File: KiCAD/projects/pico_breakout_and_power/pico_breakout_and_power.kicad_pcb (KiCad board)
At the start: 2 copper layers, 3 parts, among them J1 Conn_01x17_Socket, J12 Conn_01x17_Socket

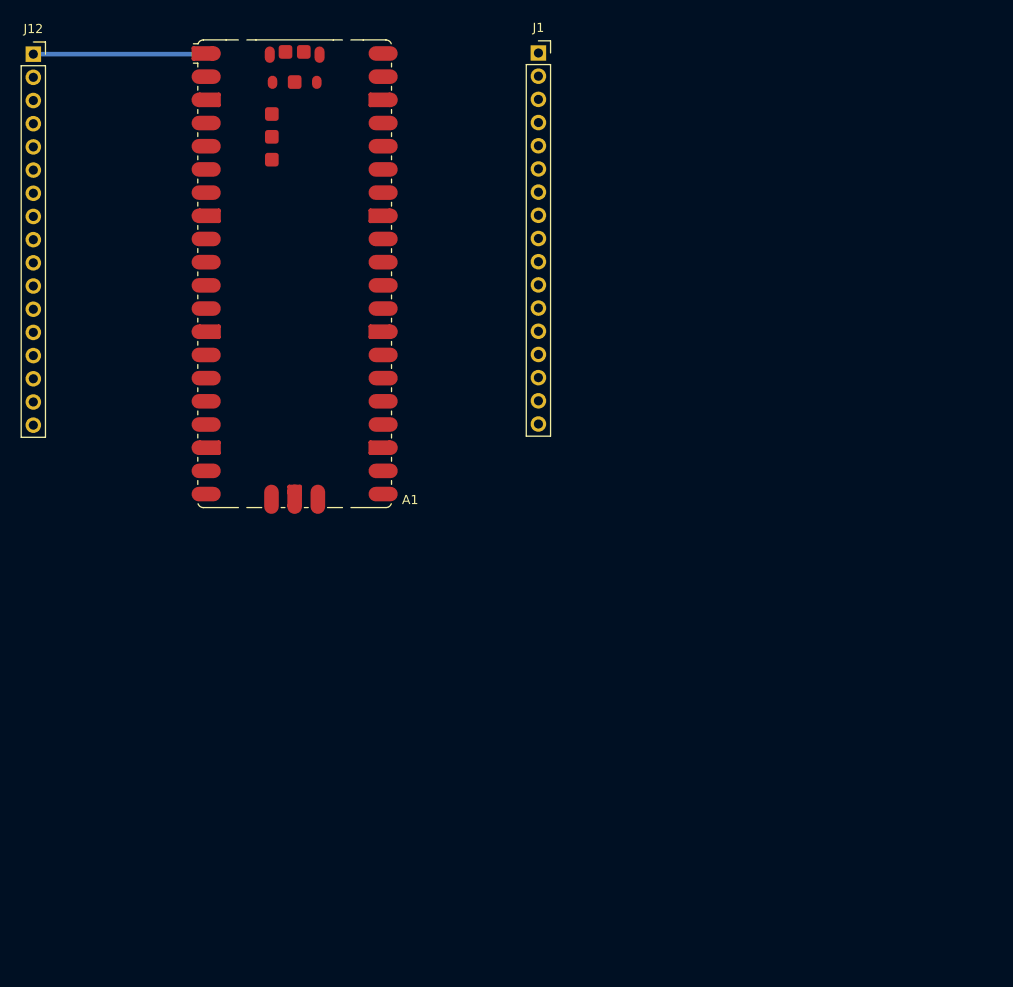
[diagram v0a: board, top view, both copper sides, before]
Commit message: Add proper board edge
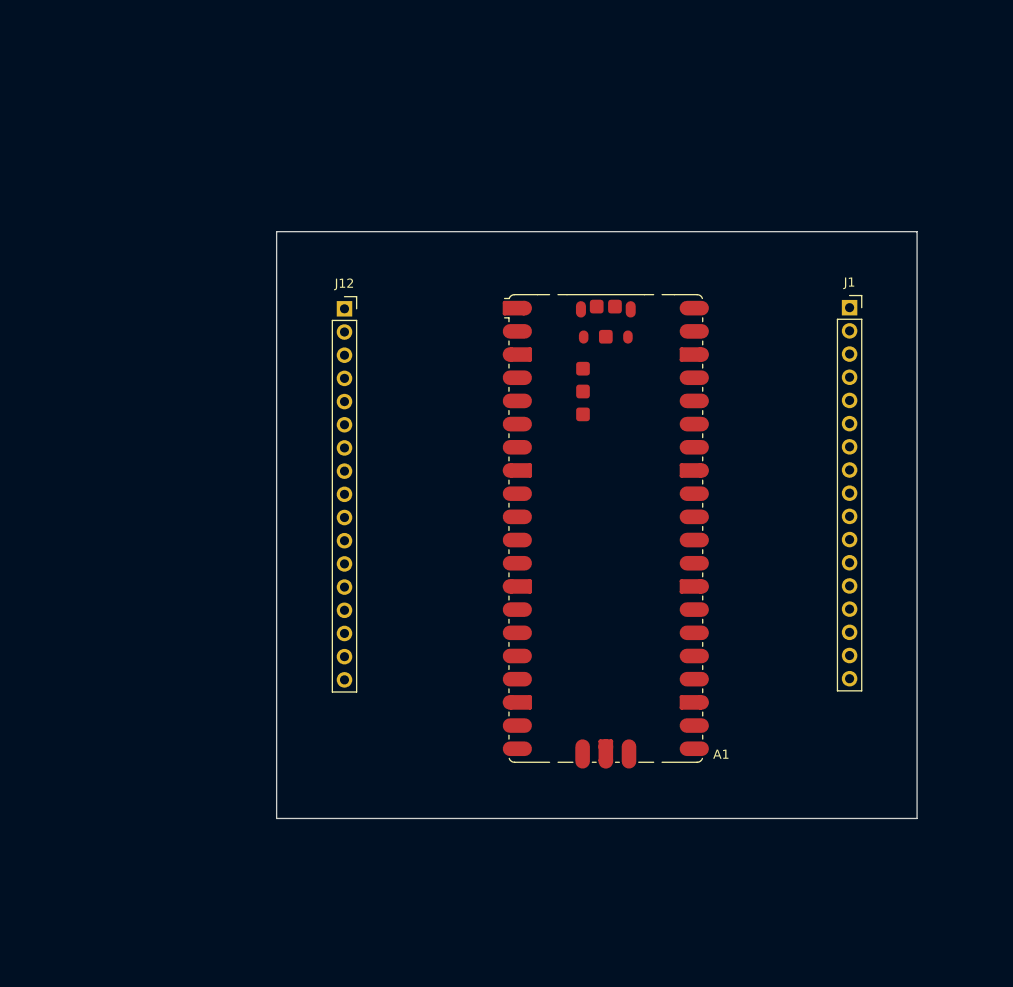
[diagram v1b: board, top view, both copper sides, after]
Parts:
- moved J1 44.0 mm to (161.6, 59.9)
- moved J12 44.0 mm to (106.3, 60.0)
- moved A1 44.0 mm to (134.9, 84.1)
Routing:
- net /GPIO0: track 19.4 -> 0.00 mm
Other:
- board outline added: 70.2 x 64.3 mm
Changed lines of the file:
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@@
 	(footprint "Module:RaspberryPi_Pico_SMD"
 		(layer "F.Cu")
-		(at 100.85 56.1875)
+		(at 134.933563 84.084311)
 		(descr "Raspberry Pi Pico (non-W) surface-mount footprint for reflow soldering with test points and debug pads, supports Raspberry Pi Pico 2 (non-W), https://datasheets.raspberrypi.com/pico/pico-datasheet.pdf")
 		(tags "module usb pcb swd")
@@
 			(polygon
 				(pts
-					(xy 100.902139 50.671955) (xy 100.936068 50.545333) (xy 101.001612 50.431806) (xy 101.094306 50.339112)
-					(xy 101.207833 50.273568) (xy 101.334455 50.239639) (xy 101.4 50.2375) (xy 101.85 50.2375) (xy 101.85 52.1375)
-					(xy 101.4 52.1375) (xy 101.334455 52.135361) (xy 101.207833 52.101432) (xy 101.094306 52.035888)
-					(xy 101.001612 51.943194) (xy 100.936068 51.829667) (xy 100.902139 51.703045) (xy 100.9 51.6375)
-					(xy 100.9 50.7375)
+					(xy 134.985702 78.568766) (xy 135.019631 78.442144) (xy 135.085175 78.328617) (xy 135.177869 78.235923)
+					(xy 135.291396 78.170379) (xy 135.418018 78.13645) (xy 135.483563 78.134311) (xy 135.933563 78.134311)
+					(xy 135.933563 80.034311) (xy 135.483563 80.034311) (xy 135.418018 80.032172) (xy 135.291396 79.998243)
+					(xy 135.177869 79.932699) (xy 135.085175 79.840005) (xy 135.019631 79.726478) (xy 134.985702 79.599856)
+					(xy 134.983563 79.534311) (xy 134.983563 78.634311)
 				)
 			)
@@
 			(polygon
 				(pts
-					(xy 101.85 52.1375) (xy 102.3 52.1375) (xy 102.365545 52.135361) (xy 102.492167 52.101433) (xy 102.605694 52.035888)
-					(xy 102.698388 51.943194) (xy 102.763933 51.829667) (xy 102.797861 51.703045) (xy 102.8 51.6375)
-					(xy 102.8 50.7375) (xy 102.797861 50.671955) (xy 102.763933 50.545333) (xy 102.698388 50.431806)
-					(xy 102.605694 50.339112) (xy 102.492167 50.273567) (xy 102.365545 50.239639) (xy 102.3 50.2375)
-					(xy 101.85 50.2375)
+					(xy 135.933563 80.034311) (xy 136.383563 80.034311) (xy 136.449108 80.032172) (xy 136.57573 79.998244)
+					(xy 136.689257 79.932699) (xy 136.781951 79.840005) (xy 136.847496 79.726478) (xy 136.881424 79.599856)
+					(xy 136.883563 79.534311) (xy 136.883563 78.634311) (xy 136.881424 78.568766) (xy 136.847496 78.442144)
+					(xy 136.781951 78.328617) (xy 136.689257 78.235923) (xy 136.57573 78.170378) (xy 136.449108 78.13645)
+					(xy 136.383563 78.134311) (xy 135.933563 78.134311)
 				)
 			)
@@
 	(footprint "Connector_PinSocket_2.54mm:PinSocket_1x17_P2.54mm_Vertical"
 		(layer "F.Cu")
-		(at 127.55 32.005)
+		(at 161.633563 59.901811)
 		(descr "Through hole straight socket strip, 1x17, 2.54mm pitch, single row (from Kicad 4.0.7), script generated")
 		(tags "Through hole socket strip THT 1x17 2.54mm single row")
@@
 	(footprint "Connector_PinSocket_2.54mm:PinSocket_1x17_P2.54mm_Vertical"
 		(layer "F.Cu")
-		(at 72.225 32.13)
+		(at 106.308563 60.026811)
 		(descr "Through hole straight socket strip, 1x17, 2.54mm pitch, single row (from Kicad 4.0.7), script generated")
 		(tags "Through hole socket strip THT 1x17 2.54mm single row")
@@
 		)
 	)
-	(segment
-		(start 72.225 32.13)
-		(end 91.295 32.13)
-		(width 0.5)
-		(layer "B.Cu")
-		(net "/GPIO0")
-	)
-	(segment
-		(start 91.295 32.13)
-		(end 91.5 31.925)
-		(width 0.5)
-		(layer "B.Cu")
-		(net "/GPIO0")
-	)
-	(zone
+	(gr_rect
+		(start 98.875 51.575)
+		(end 169.025 115.85)
+		(stroke
+			(width 0.05)
+			(type default)
+		)
+		(fill no)
 		(layer "Edge.Cuts")
-		(hatch edge 0.5)
-		(connect_pads
-			(clearance 0)
-		)
-		(min_thickness 0.25)
-		(keepout
-			(tracks not_allowed)
-			(vias not_allowed)
-			(pads not_allowed)
-			(copperpour allowed)
-			(footprints allowed)
-		)
-		(placement
-			(enabled no)
-			(sheetname "")
-		)
-		(fill
-			(thermal_gap 0.5)
-			(thermal_bridge_width 0.5)
-			(island_removal_mode 0)
-		)
-		(polygon
-			(pts
-				(xy 67.35 27.725) (xy 140.675 27.725) (xy 140.675 89.25) (xy 67.35 89.25)
-			)
-		)
 	)
 	(embedded_fonts no)

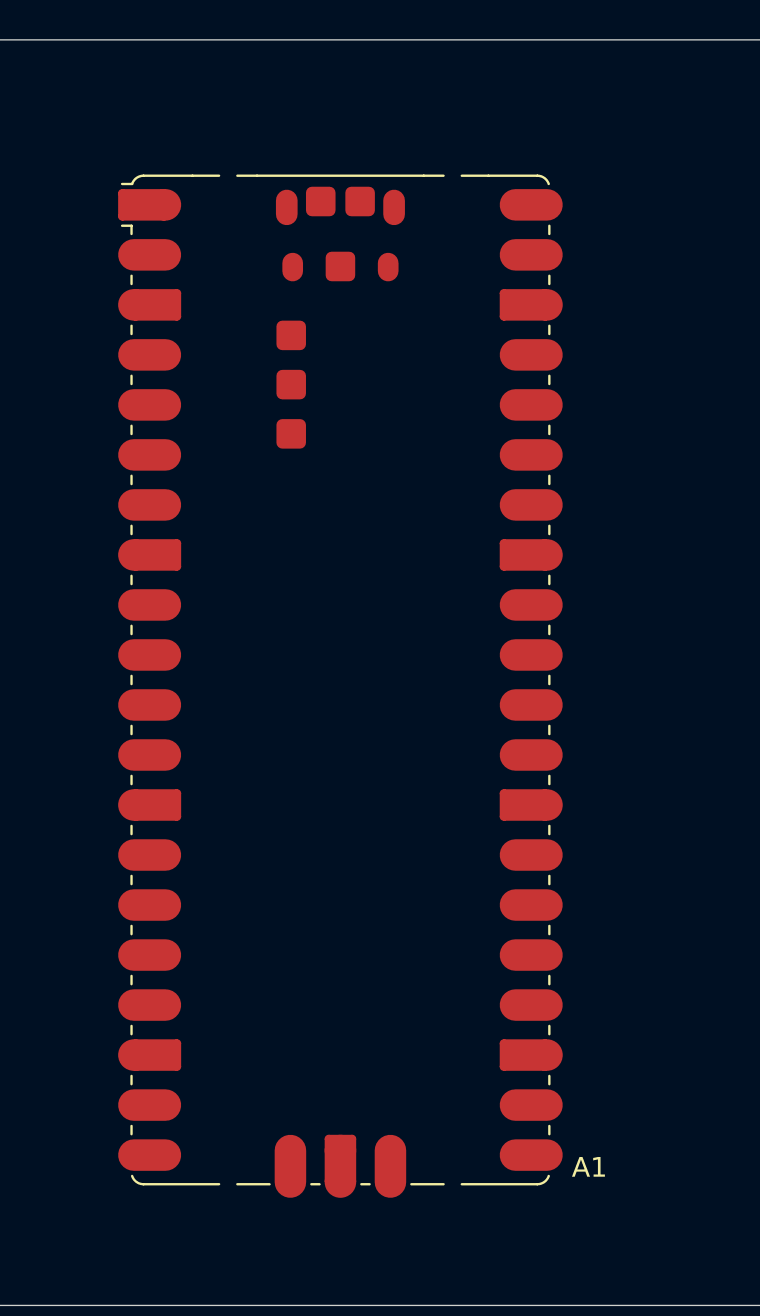
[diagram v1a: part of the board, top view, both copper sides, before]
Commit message: Made grouped 3d model of pico with sockets
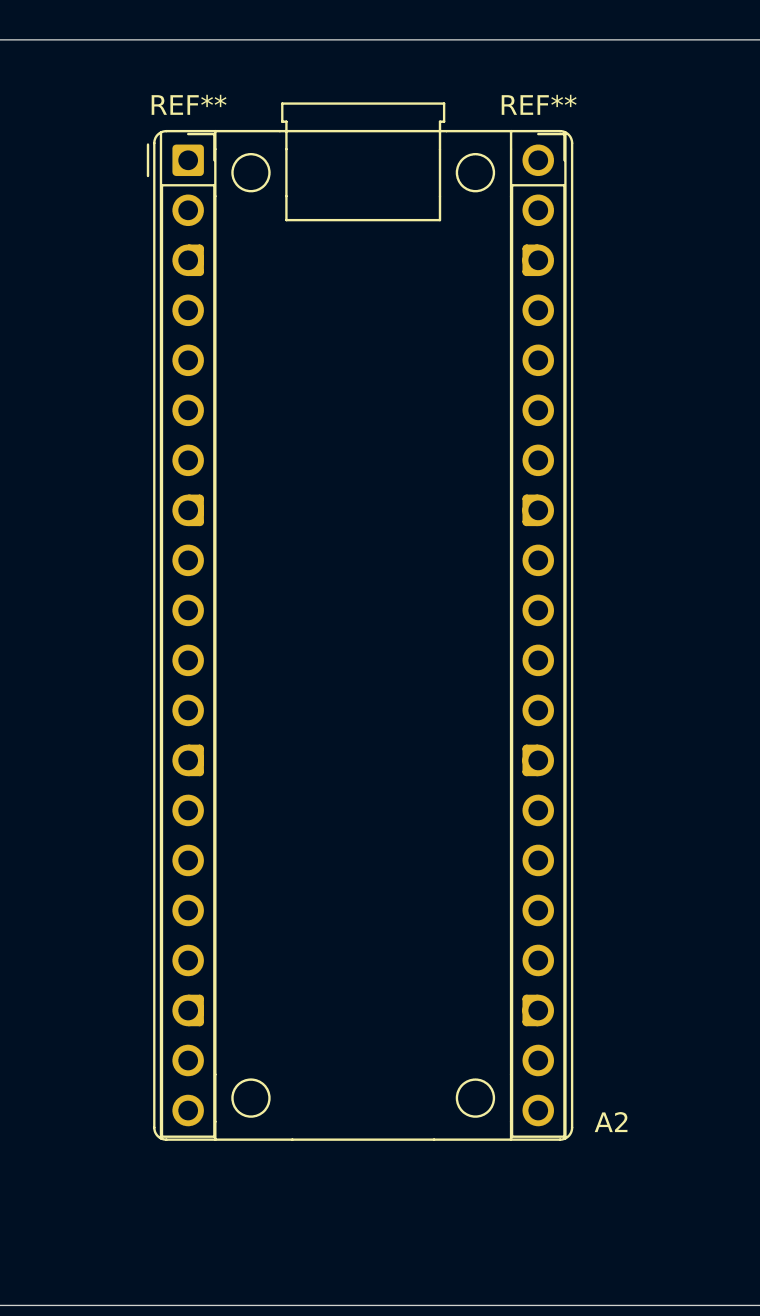
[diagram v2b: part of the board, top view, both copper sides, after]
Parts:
- removed A1: RaspberryPi_Pico, Module:RaspberryPi_Pico_SMD
- added A2: RaspberryPi_Pico, Module_RaspberryPi_Pico:RaspberryPi_Pico_Common_THT, F.Cu at (136.1, 81.8)
- added REF**: PinSocket_1x20_P2.54mm_Vertical, Connector_PinSocket_2.54mm:PinSocket_1x20_P2.54mm_Vertical, F.Cu at (127.2, 57.7)
- added REF**: PinSocket_1x20_P2.54mm_Vertical, Connector_PinSocket_2.54mm:PinSocket_1x20_P2.54mm_Vertical, F.Cu at (145.0, 57.7)

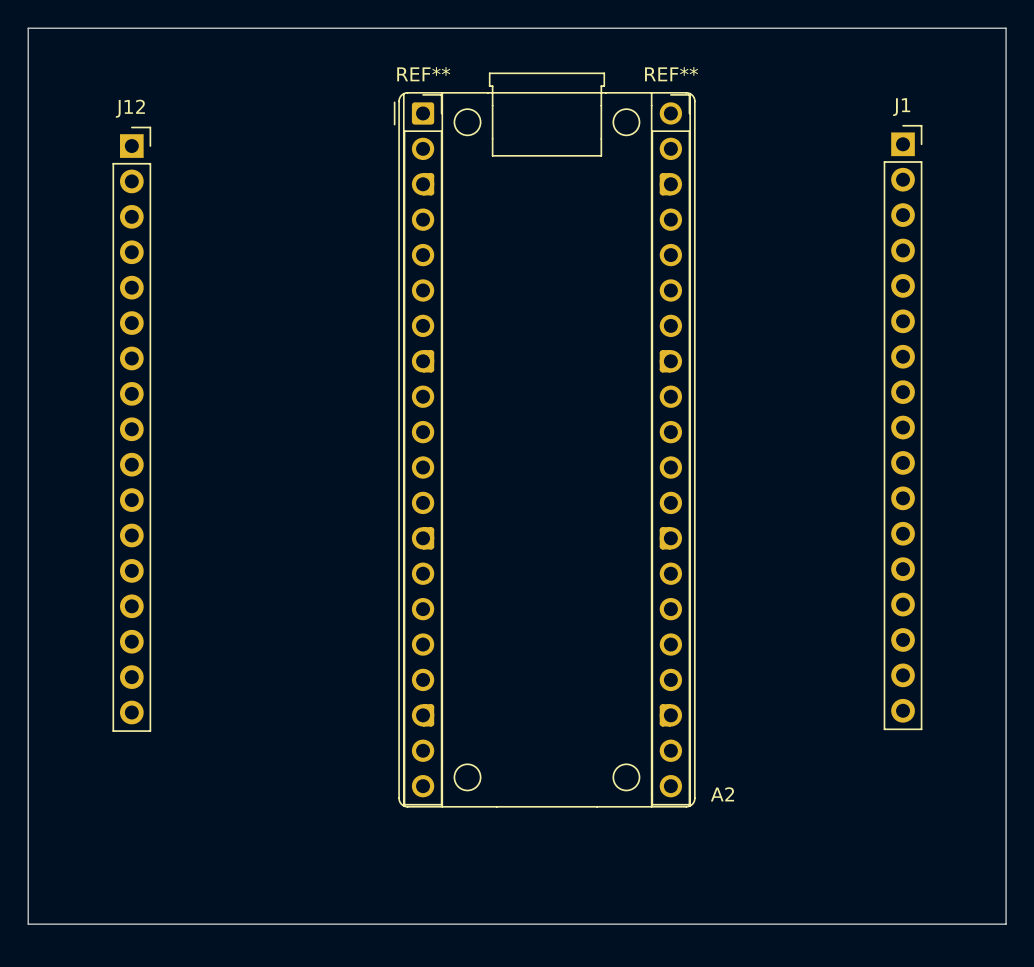
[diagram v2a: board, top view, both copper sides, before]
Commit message: Combining pico and LED driver circuits
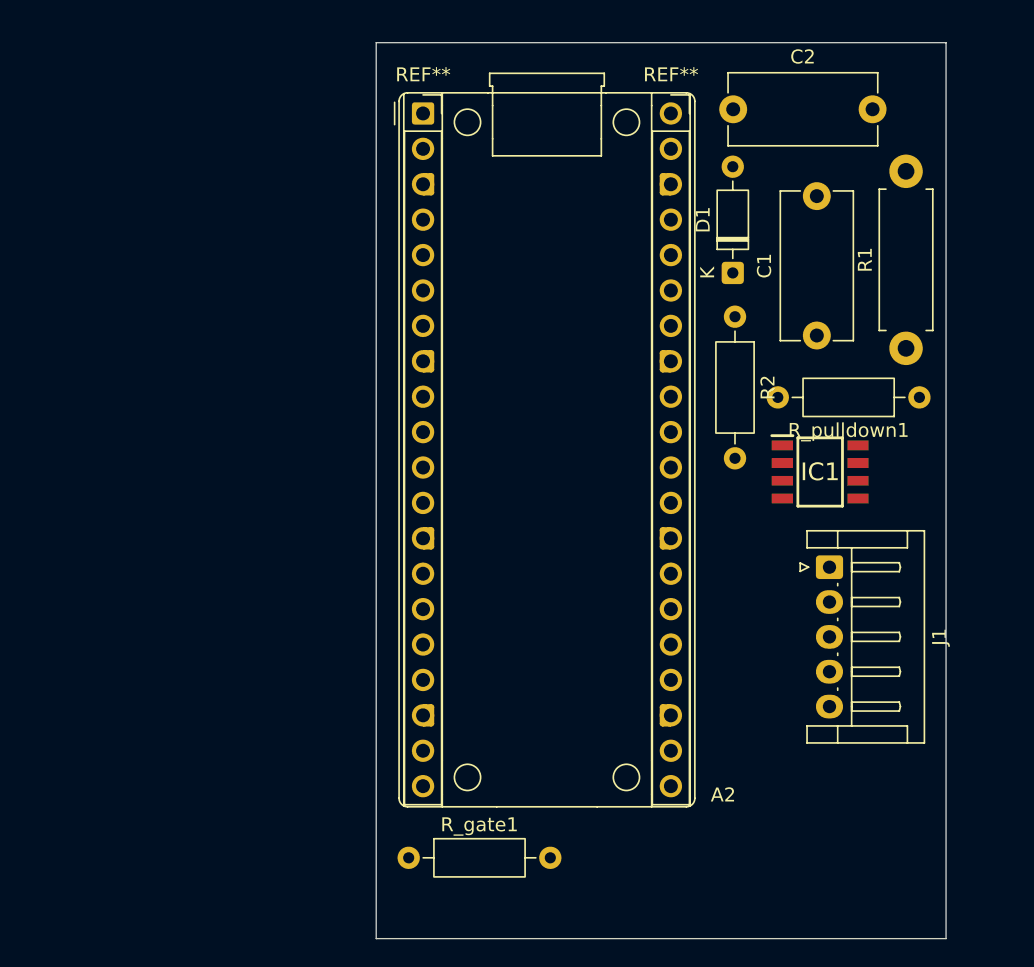
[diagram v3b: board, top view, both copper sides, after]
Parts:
- removed J12: Conn_01x17_Socket, Connector_PinSocket_2.54mm:PinSocket_1x17_P2.54mm_Vertical
- added C1: 0.47u, Capacitor_THT:C_Disc_D10.5mm_W5.0mm_P10.00mm, F.Cu at (155.4, 73.6)
- added C2: 1u, Capacitor_THT:C_Disc_D10.5mm_W5.0mm_P10.00mm, F.Cu at (149.4, 57.4)
- added D1: BAT46, Diode_THT:D_DO-35_SOD27_P7.62mm_Horizontal, F.Cu at (149.4, 69.1)
- added IC1: STCS05DR, Aidan_DST_footprints:SOIC127P600X175-8N, F.Cu at (155.7, 83.4)
- added R1: 0.22, Resistor_THT:R_Axial_DIN0411_L9.9mm_D3.6mm_P12.70mm_Horizontal, F.Cu at (161.8, 74.5)
- added R2: 100, Resistor_THT:R_Axial_DIN0207_L6.3mm_D2.5mm_P10.16mm_Horizontal, F.Cu at (149.6, 72.3)
- added R_gate1: 100, Resistor_THT:R_Axial_DIN0207_L6.3mm_D2.5mm_P10.16mm_Horizontal, F.Cu at (126.2, 111.1)
- added R_pulldown1: 100k, Resistor_THT:R_Axial_DIN0207_L6.3mm_D2.5mm_P10.16mm_Horizontal, F.Cu at (162.8, 78.1)
- J1: value Conn_01x17_Socket -> Conn_01x05_Socket; footprint Connector_PinSocket_2.54mm:PinSocket_1x17_P2.54mm_Vertical -> Connector_JST:JST_EH_S5B-EH_1x05_P2.50mm_Horizontal
- moved J1 30.8 mm to (156.4, 90.2), turned to -90 degrees
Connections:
- A2 pad 40: /VBUS -> /Anode
- J1 pad 1: /VBUS -> /3V3(OUT)
- J1 pad 2: /VSYS -> /GPIO28_ADC2
- J1 pad 3: /3V3_EN -> GND
- J1 pad 4: /3V3(OUT) -> /Anode
- J1 pad 5: /ADC_VREF -> /Cathode
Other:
- board size 70.2 x 64.3 mm -> 40.9 x 64.3 mm
